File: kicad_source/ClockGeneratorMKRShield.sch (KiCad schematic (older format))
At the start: 3 parts, among them CN1 ARDUINO_MKR

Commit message: updated schematic
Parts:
- added C? (x18): C_0603, capacitors:C_0603, symbol devices:C_0603
- added CN? (x3): 60312202114509, CON_wuerth:WR-SMA-PCB, symbol CON_wuerth:60312202114509
- added L? (x9): INDUCTOR_SMALL, L_filter:WE-CAIR_4248, symbol devices:INDUCTOR_SMALL
- added U?: SI5351A, SSOP:MSOP-10_3x3mm_Pitch0.5mm, symbol IC_interface_i2c:SI5351A
- added Y?: Crystal_Small, symbol devices:Crystal_Small
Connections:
- net SPI_MOSI: now reaches CN1.17 (8/MOSI)
- net SPI_SCK: now reaches CN1.18 (9/SCK)
- net SPI_MISO: now reaches CN1.19 (10/MISO)
- net I2C_SDA: now reaches CN1.20 (11/SDA)
- net I2C_SDA: now also U?.5 (SDA)
- net I2C_SCL: now reaches CN1.21 (12/SCL)
- net I2C_SCL: now also U?.4 (SCL)
- net SERIAL_RX: now reaches CN1.22 (13/RX)
- net SERIAL_TX: now reaches CN1.23 (14/TX)
- net RESET: now reaches CN1.24 (RESET)
- net GND: now reaches CN1.25 (GND)
- net GND: now also C?.1, C?.1, C?.1, C?.1, C?.1, C?.1, C?.1, C?.1, C?.1, C?.1, C?.1, C?.1, C?.2, C?.2, C?.2, CN?.2, CN?.2, CN?.2, CN?.3, CN?.3, CN?.3, CN?.4, CN?.4, CN?.4, CN?.5, CN?.5, CN?.5, U?.8 (GND)
- net +3V3: now reaches CN1.26 (VCC)
- net +3V3: now also C?.1, U?.1 (VDD), U?.7 (VDDO)
- net +5V: now reaches CN1.28 (5V0)
- new net: C?.2, U?.10 (CLK0)
- new net: C?.1, U?.3 (XB), Y?.2
- new net: C?.2, U?.6 (CLK2)
- new net: C?.2, U?.9 (CLK1)
- new net: C?.1, Y?.1
- new net: C?.1, C?.2, L?.1 (x3)
- new net: C?.2, L?.1, L?.2 (x6)
- new net: C?.2, CN?.1, L?.2 (x3)
- no-connect marks 0 -> 23
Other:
- moved on the sheet: CN1, L1, L2

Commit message: generated layout
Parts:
- removed C? (x4): C_0603, capacitors:C_0603, symbol devices:C_0603
- removed CN?: 60312202114509, CON_wuerth:WR-SMA-PCB, symbol CON_wuerth:60312202114509
- removed L? (x3): INDUCTOR_SMALL, L_filter:WE-CAIR_4248, symbol devices:INDUCTOR_SMALL
- removed Y?: Crystal_Small, symbol devices:Crystal_Small
- added R1, R2: 10k, resistors:R_0603, symbol devices:R_0603
- added W1: TEST_1P, wire_pads:SolderWirePad_single_0-8mmDrill, symbol mechanical-connectors:TEST_1P
- added Y1: Crystal_SMD_4Pad, crystals:Crystal_SMD_3.2x2.5mm_4Pad, symbol devices:Crystal_SMD_4Pad
- C1, C2: renamed from C?; value C_0603 -> 6.8 pF
- C3: renamed from C?; value C_0603 -> 100 nF
- gave numbers to parts that had none: 20
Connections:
- net +3V3: now also R1.1, R2.1
- net GND: now also Y1.2 (case), Y1.4 (case)
- net I2C_SCL: now also R1.2
- net I2C_SDA: now also R2.2
- net CLK0: now reaches C4.2, U1.10 (CLK0)
- net XA: now reaches U1.2 (XA)
- net XA: now also C1.1, Y1.1
- net XB: now reaches C2.1, U1.3 (XB)
- net XB: now also Y1.3
- net CLK2: now reaches C6.2, U1.6 (CLK2)
- net CLK1: now reaches C5.2, U1.9 (CLK1)
- net at C6.1: now also W1.1
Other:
- note added: "use 25 MHz crystal"
- moved on the sheet: C1

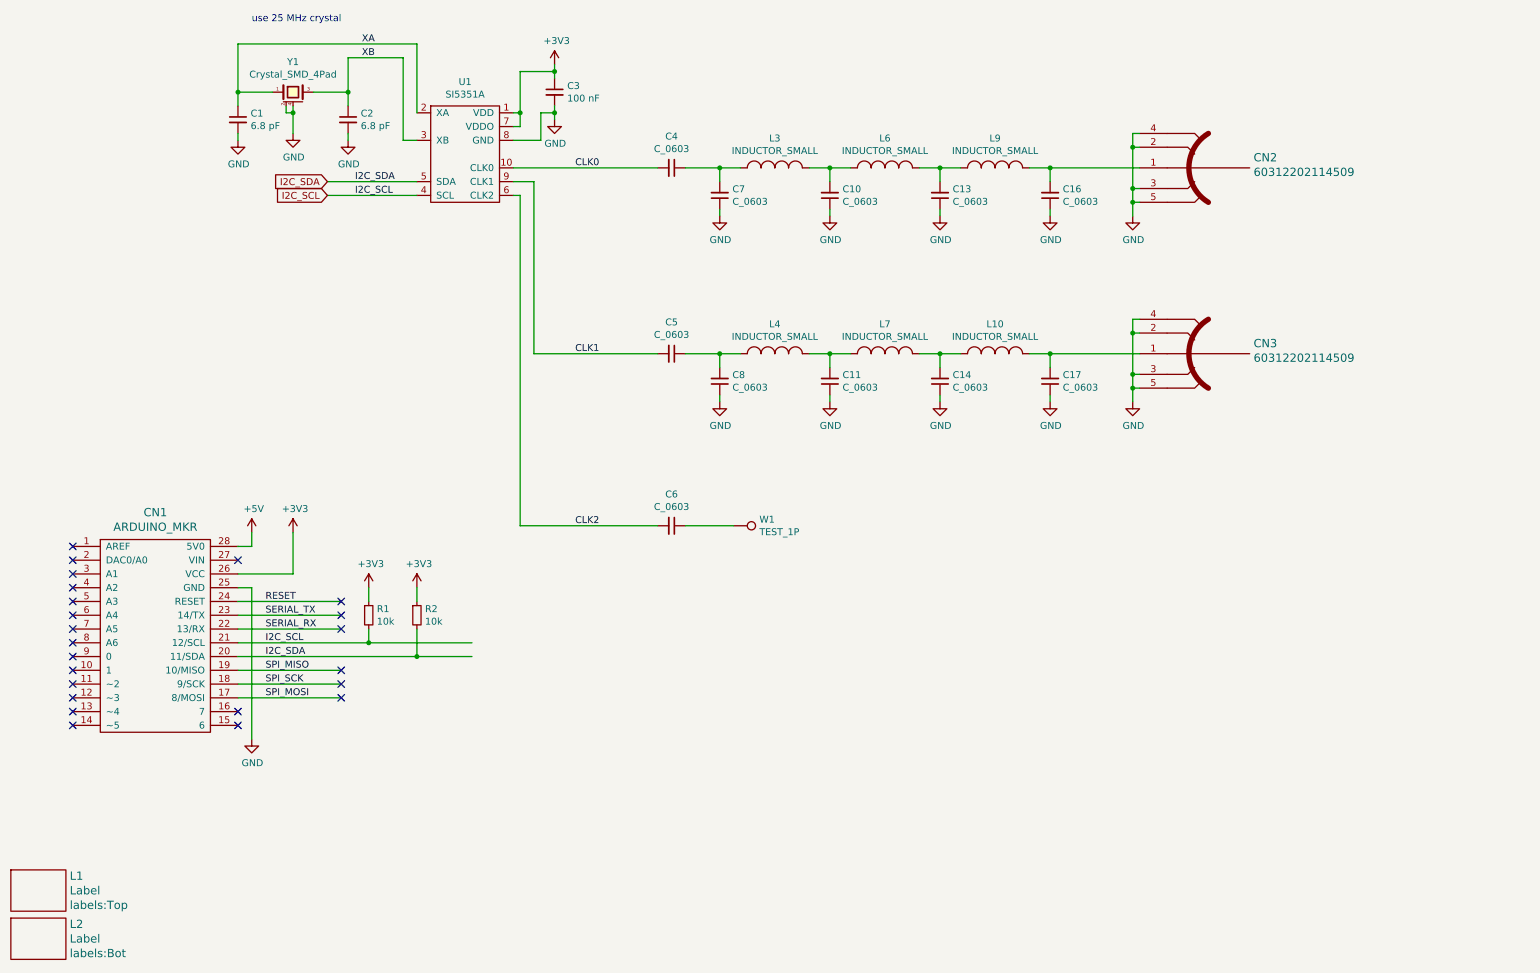
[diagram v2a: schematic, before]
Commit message: added values for filter components
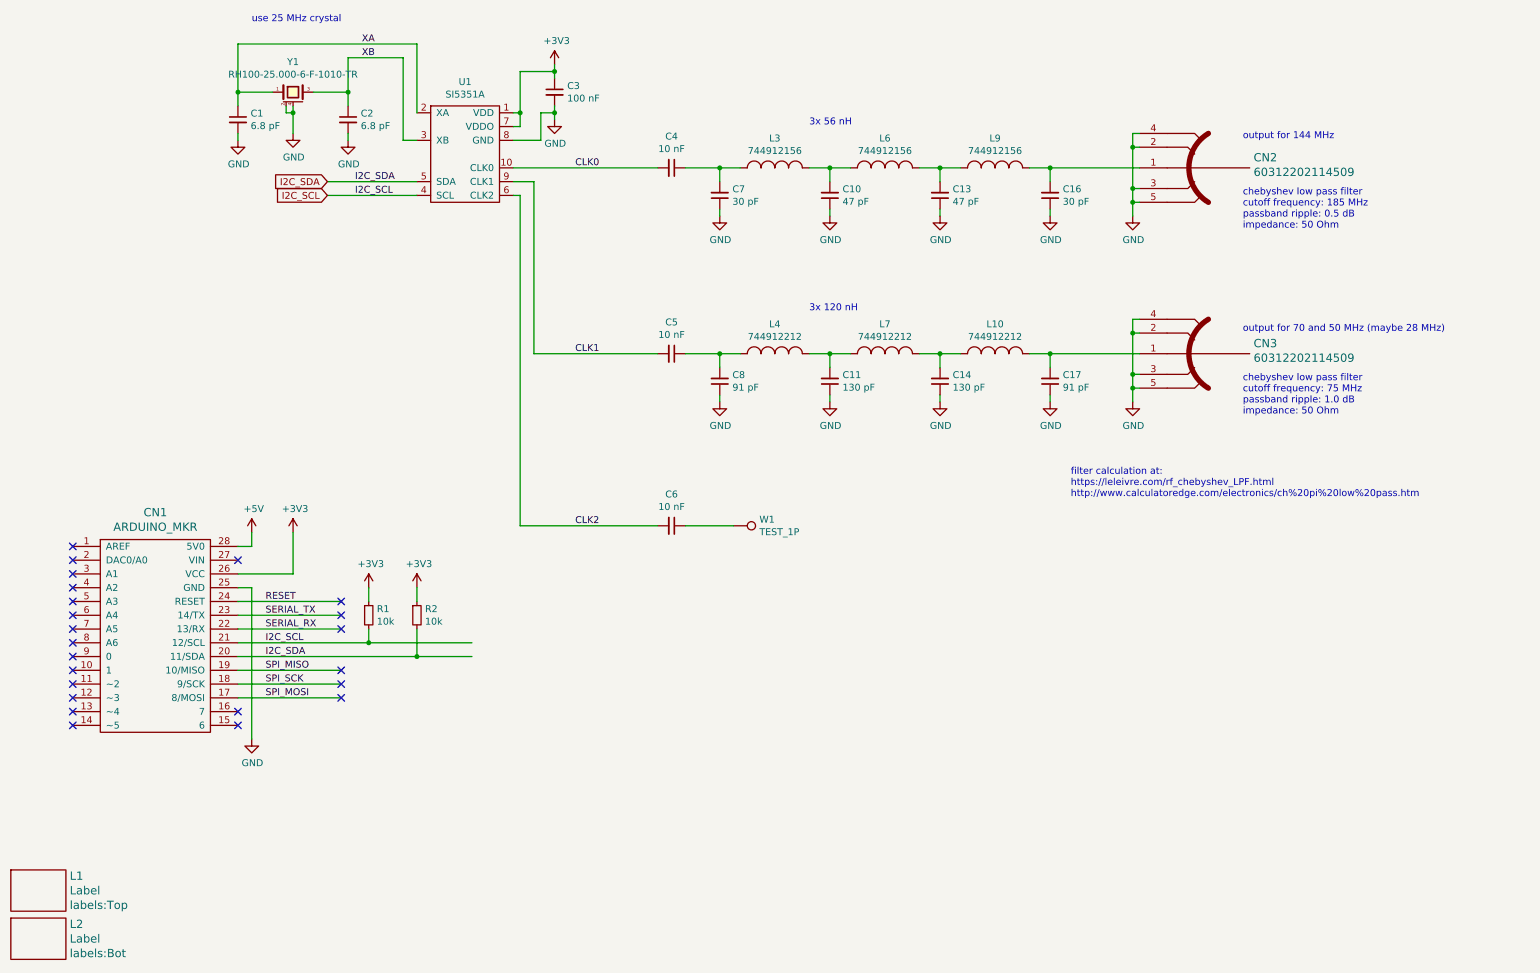
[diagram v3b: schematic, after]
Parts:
- C10, C13: value C_0603 -> 47 pF
- C11, C14: value C_0603 -> 130 pF
- C16, C7: value C_0603 -> 30 pF
- C17, C8: value C_0603 -> 91 pF
- C4, C5, C6: value C_0603 -> 10 nF
- L10, L4, L7: value INDUCTOR_SMALL -> 744912212
- L3, L6, L9: value INDUCTOR_SMALL -> 744912156
- Y1: value Crystal_SMD_4Pad -> RH100-25.000-6-F-1010-TR
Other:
- note added: "3x 120 nH"
- note added: "3x 56 nH"
- note added: "chebyshev low pass filter\ncutoff frequency: 185 MHz\npassband ripple: 0.5 dB\nimpedance: 50 Ohm"
- note added: "chebyshev low pass filter\ncutoff frequency: 75 MHz\npassband ripple: 1.0 dB\nimpedance: 50 Ohm"
- note added: "filter calculation at:\nhttps://leleivre.com/rf_chebyshev_LPF.html\nhttp://www.calculatoredge.com/electronics/ch%20pi%20low%20pass.htm"
- note added: "output for 144 MHz"
- note added: "output for 70 and 50 MHz (maybe 28 MHz)"
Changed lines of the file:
@@
 P 5300 2000
 F 0 "C4" V 5071 2000 50  0000 C CNN
-F 1 "C_0603" V 5162 2000 50  0000 C CNN
+F 1 "10 nF" V 5162 2000 50  0000 C CNN
 F 2 "capacitors:C_0603" H 5300 1850 50  0001 C CNN
 F 3 "" H 5300 2000 50  0000 C CNN
@@
 P 5650 2200
 F 0 "C7" H 5558 2154 50  0000 R CNN
-F 1 "C_0603" H 5558 2245 50  0000 R CNN
+F 1 "30 pF" H 5558 2245 50  0000 R CNN
 F 2 "capacitors:C_0603" H 5650 2050 50  0001 C CNN
 F 3 "" H 5650 2200 50  0000 C CNN
@@
 P 6050 2000
 F 0 "L3" H 6050 2215 50  0000 C CNN
-F 1 "INDUCTOR_SMALL" H 6050 2124 50  0000 C CNN
+F 1 "744912156" H 6050 2124 50  0000 C CNN
 F 2 "L_filter:WE-CAIR_4248" H 6050 2000 50  0001 C CNN
 F 3 "" H 6050 2000 50  0000 C CNN
@@
 P 6450 2200
 F 0 "C10" H 6358 2154 50  0000 R CNN
-F 1 "C_0603" H 6358 2245 50  0000 R CNN
+F 1 "47 pF" H 6358 2245 50  0000 R CNN
 F 2 "capacitors:C_0603" H 6450 2050 50  0001 C CNN
 F 3 "" H 6450 2200 50  0000 C CNN
@@
 P 6850 2000
 F 0 "L6" H 6850 2215 50  0000 C CNN
-F 1 "INDUCTOR_SMALL" H 6850 2124 50  0000 C CNN
+F 1 "744912156" H 6850 2124 50  0000 C CNN
 F 2 "L_filter:WE-CAIR_4248" H 6850 2000 50  0001 C CNN
 F 3 "" H 6850 2000 50  0000 C CNN
@@
 P 7250 2200
 F 0 "C13" H 7158 2154 50  0000 R CNN
-F 1 "C_0603" H 7158 2245 50  0000 R CNN
+F 1 "47 pF" H 7158 2245 50  0000 R CNN
 F 2 "capacitors:C_0603" H 7250 2050 50  0001 C CNN
 F 3 "" H 7250 2200 50  0000 C CNN
@@
 P 7650 2000
 F 0 "L9" H 7650 2215 50  0000 C CNN
-F 1 "INDUCTOR_SMALL" H 7650 2124 50  0000 C CNN
+F 1 "744912156" H 7650 2124 50  0000 C CNN
 F 2 "L_filter:WE-CAIR_4248" H 7650 2000 50  0001 C CNN
 F 3 "" H 7650 2000 50  0000 C CNN
@@
 P 8050 2200
 F 0 "C16" H 7958 2154 50  0000 R CNN
-F 1 "C_0603" H 7958 2245 50  0000 R CNN
+F 1 "30 pF" H 7958 2245 50  0000 R CNN
 F 2 "capacitors:C_0603" H 8050 2050 50  0001 C CNN
 F 3 "" H 8050 2200 50  0000 C CNN
@@
 P 5300 3350
 F 0 "C5" V 5071 3350 50  0000 C CNN
-F 1 "C_0603" V 5162 3350 50  0000 C CNN
+F 1 "10 nF" V 5162 3350 50  0000 C CNN
 F 2 "capacitors:C_0603" H 5300 3200 50  0001 C CNN
 F 3 "" H 5300 3350 50  0000 C CNN
@@
 P 5650 3550
 F 0 "C8" H 5558 3504 50  0000 R CNN
-F 1 "C_0603" H 5558 3595 50  0000 R CNN
+F 1 "91 pF" H 5558 3595 50  0000 R CNN
 F 2 "capacitors:C_0603" H 5650 3400 50  0001 C CNN
 F 3 "" H 5650 3550 50  0000 C CNN
@@
 P 6050 3350
 F 0 "L4" H 6050 3565 50  0000 C CNN
-F 1 "INDUCTOR_SMALL" H 6050 3474 50  0000 C CNN
+F 1 "744912212" H 6050 3474 50  0000 C CNN
 F 2 "L_filter:WE-CAIR_4248" H 6050 3350 50  0001 C CNN
 F 3 "" H 6050 3350 50  0000 C CNN
@@
 P 6450 3550
 F 0 "C11" H 6358 3504 50  0000 R CNN
-F 1 "C_0603" H 6358 3595 50  0000 R CNN
+F 1 "130 pF" H 6358 3595 50  0000 R CNN
 F 2 "capacitors:C_0603" H 6450 3400 50  0001 C CNN
 F 3 "" H 6450 3550 50  0000 C CNN
@@
 P 6850 3350
 F 0 "L7" H 6850 3565 50  0000 C CNN
-F 1 "INDUCTOR_SMALL" H 6850 3474 50  0000 C CNN
+F 1 "744912212" H 6850 3474 50  0000 C CNN
 F 2 "L_filter:WE-CAIR_4248" H 6850 3350 50  0001 C CNN
 F 3 "" H 6850 3350 50  0000 C CNN
@@
 P 7250 3550
 F 0 "C14" H 7158 3504 50  0000 R CNN
-F 1 "C_0603" H 7158 3595 50  0000 R CNN
+F 1 "130 pF" H 7158 3595 50  0000 R CNN
 F 2 "capacitors:C_0603" H 7250 3400 50  0001 C CNN
 F 3 "" H 7250 3550 50  0000 C CNN
@@
 P 7650 3350
 F 0 "L10" H 7650 3565 50  0000 C CNN
-F 1 "INDUCTOR_SMALL" H 7650 3474 50  0000 C CNN
+F 1 "744912212" H 7650 3474 50  0000 C CNN
 F 2 "L_filter:WE-CAIR_4248" H 7650 3350 50  0001 C CNN
 F 3 "" H 7650 3350 50  0000 C CNN
@@
 P 8050 3550
 F 0 "C17" H 7958 3504 50  0000 R CNN
-F 1 "C_0603" H 7958 3595 50  0000 R CNN
+F 1 "91 pF" H 7958 3595 50  0000 R CNN
 F 2 "capacitors:C_0603" H 8050 3400 50  0001 C CNN
 F 3 "" H 8050 3550 50  0000 C CNN
@@
 P 5300 4600
 F 0 "C6" V 5071 4600 50  0000 C CNN
-F 1 "C_0603" V 5162 4600 50  0000 C CNN
+F 1 "10 nF" V 5162 4600 50  0000 C CNN
 F 2 "capacitors:C_0603" H 5300 4450 50  0001 C CNN
 F 3 "" H 5300 4600 50  0000 C CNN
@@
 P 2550 1450
 F 0 "Y1" H 2550 1670 50  0000 C CNN
-F 1 "Crystal_SMD_4Pad" H 2550 1579 50  0000 C CNN
+F 1 "RH100-25.000-6-F-1010-TR" H 2550 1579 50  0000 C CNN
 F 2 "crystals:Crystal_SMD_3.2x2.5mm_4Pad" H 2550 1250 50  0001 C CNN
 F 3 "" H 2550 1450 50  0000 C CNN
@@
 Wire Wire Line
 	5400 4600 5750 4600
+Text Notes 9450 1800 0    50   ~ 0
+output for 144 MHz
+Text Notes 9450 3200 0    50   ~ 0
+output for 70 and 50 MHz (maybe 28 MHz)
+Text Notes 6300 3050 0    50   ~ 0
+3x 120 nH
+Text Notes 6300 1700 0    50   ~ 0
+3x 56 nH
+Text Notes 9450 2450 0    50   ~ 0
+chebyshev low pass filter\ncutoff frequency: 185 MHz\npassband ripple: 0.5 dB\nimpedance: 50 Ohm
+Text Notes 9450 3800 0    50   ~ 0
+chebyshev low pass filter\ncutoff frequency: 75 MHz\npassband ripple: 1.0 dB\nimpedance: 50 Ohm
+Text Notes 8200 4400 0    50   ~ 0
+filter calculation at:\nhttps://leleivre.com/rf_chebyshev_LPF.html\nhttp://www.calculatoredge.com/electronics/ch%20pi%20low%20pass.htm
 $EndSCHEMATC

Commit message: added connector for gps module
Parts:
- added CN4: SM04B-SRSS-TB, Connector_JST:JST_SH_SM04B-SRSS-TB_1x04-1MP_P1.00mm_Horizontal, symbol mechanical-connectors:CONN_01X04
- added W2: TEST_1P, wire_pads:SolderWirePad_single_0-8mmDrill, symbol mechanical-connectors:TEST_1P
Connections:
- net labels added: PPS_INT
- wire segments 107 -> 115
- no-connect marks 23 -> 20
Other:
- note added: "for GPS"
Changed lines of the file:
@@
 	4200 2200 4200 4600
 NoConn ~ 950  6050
-NoConn ~ 950  5950
 NoConn ~ 950  5850
 NoConn ~ 950  5750
@@
 NoConn ~ 2900 5750
 NoConn ~ 2900 5650
-NoConn ~ 2900 5350
-NoConn ~ 2900 5250
 NoConn ~ 2900 5150
 $Comp
@@
 Text Notes 8200 4400 0    50   ~ 0
 filter calculation at:\nhttps://leleivre.com/rf_chebyshev_LPF.html\nhttp://www.calculatoredge.com/electronics/ch%20pi%20low%20pass.htm
+$Comp
+L mechanical-connectors:CONN_01X04 CN4
+U 1 1 6028D343
+P 3150 7100
+F 0 "CN4" H 3228 7141 50  0000 L CNN
+F 1 "SM04B-SRSS-TB" H 3228 7050 50  0000 L CNN
+F 2 "Connector_JST:JST_SH_SM04B-SRSS-TB_1x04-1MP_P1.00mm_Horizontal" H 3228 7004 50  0001 L CNN
+F 3 "" H 3150 7100 50  0000 C CNN
+	1    3150 7100
+	1    0    0    -1
+$EndComp
+$Comp
+L power-supply:GND #PWR016
+U 1 1 6028D857
+P 2850 7350
+F 0 "#PWR016" H 2850 7100 50  0001 C CNN
+F 1 "GND" H 2855 7177 50  0000 C CNN
+F 2 "" H 2850 7350 50  0000 C CNN
+F 3 "" H 2850 7350 50  0000 C CNN
+	1    2850 7350
+	1    0    0    -1
+$EndComp
+$Comp
+L power-supply:+3V3 #PWR013
+U 1 1 6028E376
+P 2750 6850
+F 0 "#PWR013" H 2750 6700 50  0001 C CNN
+F 1 "+3V3" H 2765 7023 50  0000 C CNN
+F 2 "" H 2750 6850 50  0000 C CNN
+F 3 "" H 2750 6850 50  0000 C CNN
+	1    2750 6850
+	1    0    0    -1
+$EndComp
+Wire Wire Line
+	2050 7150 2950 7150
+Wire Wire Line
+	2050 7250 2950 7250
+Wire Wire Line
+	2950 6950 2850 6950
+Wire Wire Line
+	2850 6950 2850 7350
+Wire Wire Line
+	2950 7050 2750 7050
+Wire Wire Line
+	2750 7050 2750 6850
+Text Label 2150 7150 0    50   ~ 0
+SERIAL_TX
+Text Label 2150 7250 0    50   ~ 0
+SERIAL_RX
+$Comp
+L mechanical-connectors:TEST_1P W2
+U 1 1 6029D1AF
+P 3100 6550
+F 0 "W2" V 3054 6738 50  0000 L CNN
+F 1 "TEST_1P" V 3145 6738 50  0000 L CNN
+F 2 "wire_pads:SolderWirePad_single_0-8mmDrill" H 3300 6550 50  0001 C CNN
+F 3 "" H 3300 6550 50  0000 C CNN
+	1    3100 6550
+	0    1    1    0
+$EndComp
+Wire Wire Line
+	2250 6550 3100 6550
+Text Label 2450 6550 0    50   ~ 0
+PPS_INT
+Wire Wire Line
+	550  5950 950  5950
+Text Label 600  5950 0    50   ~ 0
+PPS_INT
+Text Notes 3750 7000 0    50   ~ 0
+for GPS
 $EndSCHEMATC
